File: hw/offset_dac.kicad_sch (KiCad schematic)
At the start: 23 parts, among them U11 TSV992A, U14 MCP47CVB02-E_UN

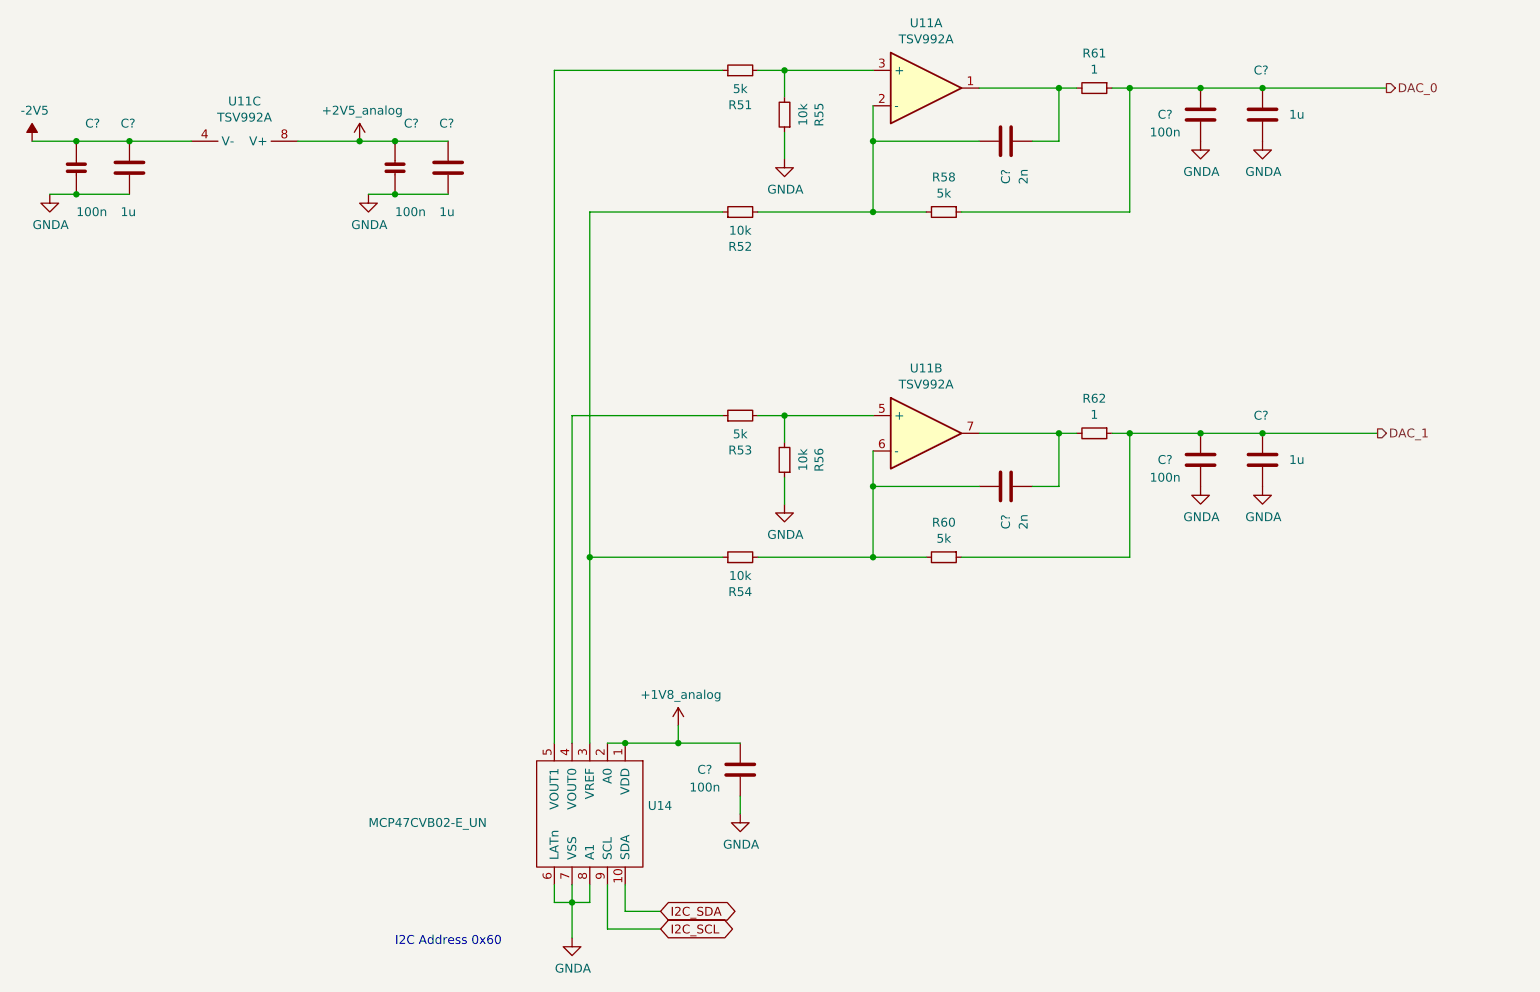
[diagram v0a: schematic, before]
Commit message: basic schematic, started layout (placing first components)
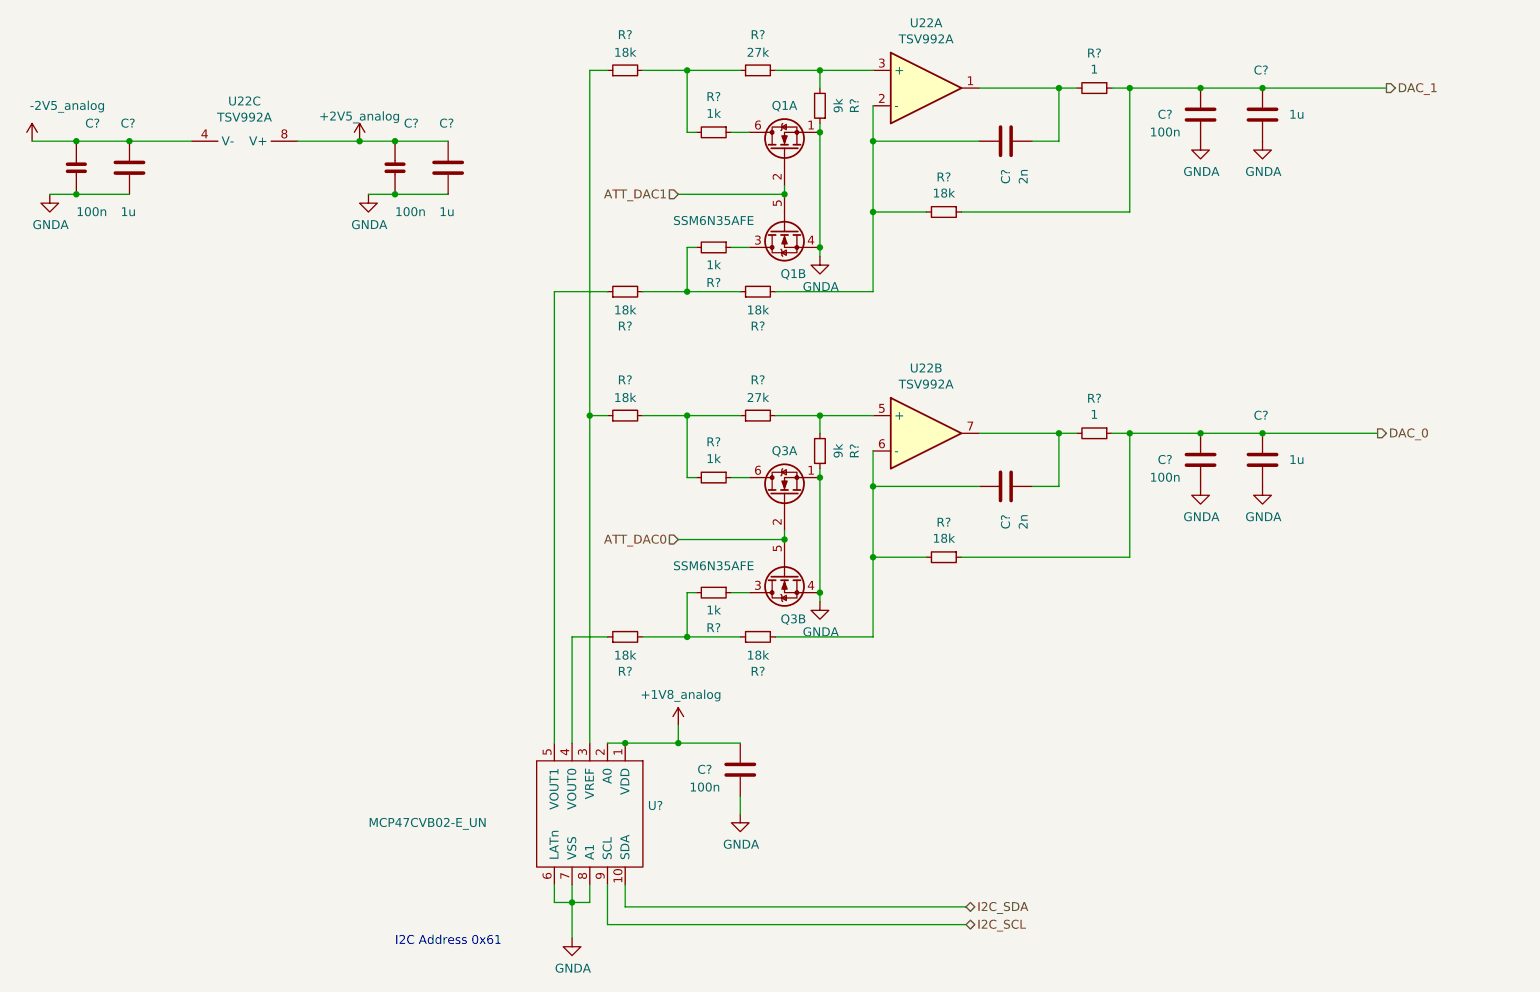
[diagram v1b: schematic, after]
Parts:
- removed R53: 5k, Resistor_SMD:R_0603_1608Metric, symbol Device:R_Small
- removed R54, R56: 10k, Resistor_SMD:R_0603_1608Metric, symbol Device:R_Small
- added Q1, Q3: SSM6N35AFE, proj_footprints:SOT-563-adjusted, symbol Device:Q_Dual_NMOS_S1G1D2S2G2D1
- added R? (x4): 1k, Resistor_SMD:R_0603_1608Metric, symbol Device:R_Small
- added R? (x4): 18k, Resistor_SMD:R_0603_1608Metric, symbol Device:R_Small
- added R? (x2): 27k, Resistor_SMD:R_0603_1608Metric, symbol Device:R_Small
- added R?: 9k, Resistor_SMD:R_0603_1608Metric, symbol Device:R_Small
- R?: renamed from R58; value 5k -> 18k
- R?: renamed from R55; value 10k -> 9k
- R?: renamed from R51; value 5k -> 18k
- R?: renamed from R52; value 10k -> 18k
- R?: renamed from R60; value 5k -> 18k
- U22: renamed from U11; symbol usbadc-rescue:Opamp_Dual_Generic-Device -> Device:Opamp_Dual
- renumbered R61 to R?, R62 to R?, U14 to U?
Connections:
- net DAC_0: now also C?.1, C?.2, R?.1, R?.1; no longer C?.1, C?.2, R?.1, R?.1
- net DAC_1: now also C?.1, C?.2, R?.1, R?.1; no longer C?.1, C?.2, R?.1, R?.1
- net GNDA: now also Q1.1 (S), Q1.4 (S), Q3.1 (S), Q3.4 (S), R?.1
- net at U?.3 (VREF): now also R?.1, R?.1; no longer R?.1
- net at U?.4 (VOUT0): now also R?.1
- net at U?.5 (VOUT1): now also R?.1; no longer R?.1
- net at C?.2, R?.2, U22.2 (-): now also R?.2; no longer R?.2
- net at R?.2, U22.3 (+): now also R?.2; no longer R?.2
- net at U22.5 (+): now also R?.2, R?.2
- net at C?.2, R?.2, U22.6 (-): now also R?.2
- net -2V5 renamed -2V5_analog
- new net: R?.1, R?.2, R?.2 (x4)
- new net: Q1.6 (D), R?.1
- new net: Q3.3 (D), R?.1
- new net: Q1.3 (D), R?.1
- new net: Q3.6 (D), R?.1
- new net ATT_DAC0: Q3.2 (G), Q3.5 (G)
- new net ATT_DAC1: Q1.2 (G), Q1.5 (G)
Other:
- note added: "I2C Address 0x61"
- note removed: "I2C Address 0x60"
- moved on the sheet: R?

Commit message: WIP - a lot already laid out.
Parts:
- C? (x2): footprint Capacitor_SMD:C_0402_1005Metric -> Capacitor_SMD:C_0603_1608Metric
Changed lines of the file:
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@@
       (effects (font (size 1.27 1.27)) (justify left))
     )
-    (property "Footprint" "Capacitor_SMD:C_0402_1005Metric" (at 78.4352 63.5 0)
+    (property "Footprint" "Capacitor_SMD:C_0603_1608Metric" (at 78.4352 63.5 0)
       (effects (font (size 1.27 1.27)) hide)
     )
@@
       (effects (font (size 1.27 1.27)) (justify left))
     )
-    (property "Footprint" "Capacitor_SMD:C_0402_1005Metric" (at 32.7152 63.5 0)
+    (property "Footprint" "Capacitor_SMD:C_0603_1608Metric" (at 32.7152 63.5 0)
       (effects (font (size 1.27 1.27)) hide)
     )

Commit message: finished routing; DRC passes (except for 1 hole violation at push-button)
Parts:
- C? (x2): Manufacturer Murata -> (none)
- C? (x3): Manufacturer Murata -> (none); Part GCJ188R71E104KA12D -> (none)
- C? (x4): Manufacturer Murata -> (none); Part GCJ219R71C105KA01 -> (none)
- C? (x2): Manufacturer Murata -> (none); Part GRM155R61C104KA88D -> (none)
- Q1, Q3: Manufacturer (none) -> Toshiba; Part (none) -> SSM6N35AFE
- Q1, Q3: Part (none) -> SSM6N35AFE
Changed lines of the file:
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@@
       (effects (font (size 1.27 1.27)) hide)
     )
-    (property "Manufacturer" "Murata" (at 172.72 61.595 0)
+    (property "Manufacturer" "" (at 172.72 61.595 0)
       (effects (font (size 1.27 1.27)) hide)
     )
@@
       (effects (font (size 1.27 1.27)) hide)
     )
-    (property "Part" "GCJ188R71E104KA12D" (at 189.865 57.15 0)
-      (effects (font (size 1.27 1.27)) hide)
-    )
-    (property "Manufacturer" "Murata" (at 187.325 59.69 0)
+    (property "Part" "" (at 189.865 57.15 0)
+      (effects (font (size 1.27 1.27)) hide)
+    )
+    (property "Manufacturer" "" (at 187.325 59.69 0)
       (effects (font (size 1.27 1.27)) hide)
     )
@@
       (effects (font (size 1.27 1.27)) hide)
     )
-    (property "Part" "GCJ219R71C105KA01" (at 205.105 46.99 0)
-      (effects (font (size 1.27 1.27)) hide)
-    )
-    (property "Manufacturer" "Murata" (at 207.645 44.45 0)
+    (property "Part" "" (at 205.105 46.99 0)
+      (effects (font (size 1.27 1.27)) hide)
+    )
+    (property "Manufacturer" "" (at 207.645 44.45 0)
       (effects (font (size 1.27 1.27)) hide)
     )
@@
       (effects (font (size 1.27 1.27)) hide)
     )
-    (property "Manufacturer" "Murata" (at 172.72 111.125 0)
+    (property "Manufacturer" "" (at 172.72 111.125 0)
       (effects (font (size 1.27 1.27)) hide)
     )
@@
       (effects (font (size 1.27 1.27)) hide)
     )
-    (property "Part" "GCJ188R71E104KA12D" (at 189.865 106.68 0)
-      (effects (font (size 1.27 1.27)) hide)
-    )
-    (property "Manufacturer" "Murata" (at 187.325 109.22 0)
+    (property "Part" "" (at 189.865 106.68 0)
+      (effects (font (size 1.27 1.27)) hide)
+    )
+    (property "Manufacturer" "" (at 187.325 109.22 0)
       (effects (font (size 1.27 1.27)) hide)
     )
@@
       (effects (font (size 1.27 1.27)) hide)
     )
-    (property "Part" "GCJ219R71C105KA01" (at 205.105 96.52 0)
-      (effects (font (size 1.27 1.27)) hide)
-    )
-    (property "Manufacturer" "Murata" (at 207.645 93.98 0)
+    (property "Part" "" (at 205.105 96.52 0)
+      (effects (font (size 1.27 1.27)) hide)
+    )
+    (property "Manufacturer" "" (at 207.645 93.98 0)
       (effects (font (size 1.27 1.27)) hide)
     )
@@
       (effects (font (size 1.27 1.27)) hide)
     )
-    (property "Part" "GCJ188R71E104KA12D" (at 123.825 151.13 0)
-      (effects (font (size 1.27 1.27)) hide)
-    )
-    (property "Manufacturer" "Murata" (at 121.285 153.67 0)
+    (property "Part" "" (at 123.825 151.13 0)
+      (effects (font (size 1.27 1.27)) hide)
+    )
+    (property "Manufacturer" "" (at 121.285 153.67 0)
       (effects (font (size 1.27 1.27)) hide)
     )
@@
       (effects (font (size 1.27 1.27)) hide)
     )
-    (property "Part" "GRM155R61C104KA88D" (at 80.645 54.61 0)
-      (effects (font (size 1.27 1.27)) hide)
-    )
-    (property "Manufacturer" "Murata" (at 83.185 52.07 0)
+    (property "Part" "" (at 80.645 54.61 0)
+      (effects (font (size 1.27 1.27)) hide)
+    )
+    (property "Manufacturer" "" (at 83.185 52.07 0)
       (effects (font (size 1.27 1.27)) hide)
     )
@@
       (effects (font (size 1.27 1.27)) hide)
     )
-    (property "Part" "GCJ219R71C105KA01" (at 88.265 54.61 0)
-      (effects (font (size 1.27 1.27)) hide)
-    )
-    (property "Manufacturer" "Murata" (at 90.805 52.07 0)
+    (property "Part" "" (at 88.265 54.61 0)
+      (effects (font (size 1.27 1.27)) hide)
+    )
+    (property "Manufacturer" "" (at 90.805 52.07 0)
       (effects (font (size 1.27 1.27)) hide)
     )
@@
       (effects (font (size 1.27 1.27)) hide)
     )
-    (property "Part" "GRM155R61C104KA88D" (at 34.925 54.61 0)
-      (effects (font (size 1.27 1.27)) hide)
-    )
-    (property "Manufacturer" "Murata" (at 37.465 52.07 0)
+    (property "Part" "" (at 34.925 54.61 0)
+      (effects (font (size 1.27 1.27)) hide)
+    )
+    (property "Manufacturer" "" (at 37.465 52.07 0)
       (effects (font (size 1.27 1.27)) hide)
     )
@@
       (effects (font (size 1.27 1.27)) hide)
     )
-    (property "Part" "GCJ219R71C105KA01" (at 42.545 54.61 0)
-      (effects (font (size 1.27 1.27)) hide)
-    )
-    (property "Manufacturer" "Murata" (at 45.085 52.07 0)
+    (property "Part" "" (at 42.545 54.61 0)
+      (effects (font (size 1.27 1.27)) hide)
+    )
+    (property "Manufacturer" "" (at 45.085 52.07 0)
       (effects (font (size 1.27 1.27)) hide)
     )
@@
     )
     (property "Datasheet" "~" (at 133.35 52.07 0)
+      (effects (font (size 1.27 1.27)) hide)
+    )
+    (property "Manufacturer" "Toshiba" (at 133.35 57.15 0)
+      (effects (font (size 1.27 1.27)) hide)
+    )
+    (property "Part" "SSM6N35AFE" (at 133.35 57.15 0)
       (effects (font (size 1.27 1.27)) hide)
     )
@@
       (effects (font (size 1.27 1.27)) hide)
     )
+    (property "Manufacturer" "Toshiba" (at 133.35 106.68 0)
+      (effects (font (size 1.27 1.27)) hide)
+    )
+    (property "Part" "SSM6N35AFE" (at 133.35 106.68 0)
+      (effects (font (size 1.27 1.27)) hide)
+    )
     (pin "1")
     (pin "2")
@@
       (effects (font (size 1.27 1.27)) hide)
     )
+    (property "Part" "SSM6N35AFE" (at 133.35 68.58 0)
+      (effects (font (size 1.27 1.27)) hide)
+    )
     (pin "1")
     (pin "2")
@@
       (effects (font (size 1.27 1.27)) hide)
     )
+    (property "Part" "SSM6N35AFE" (at 133.35 118.11 0)
+      (effects (font (size 1.27 1.27)) hide)
+    )

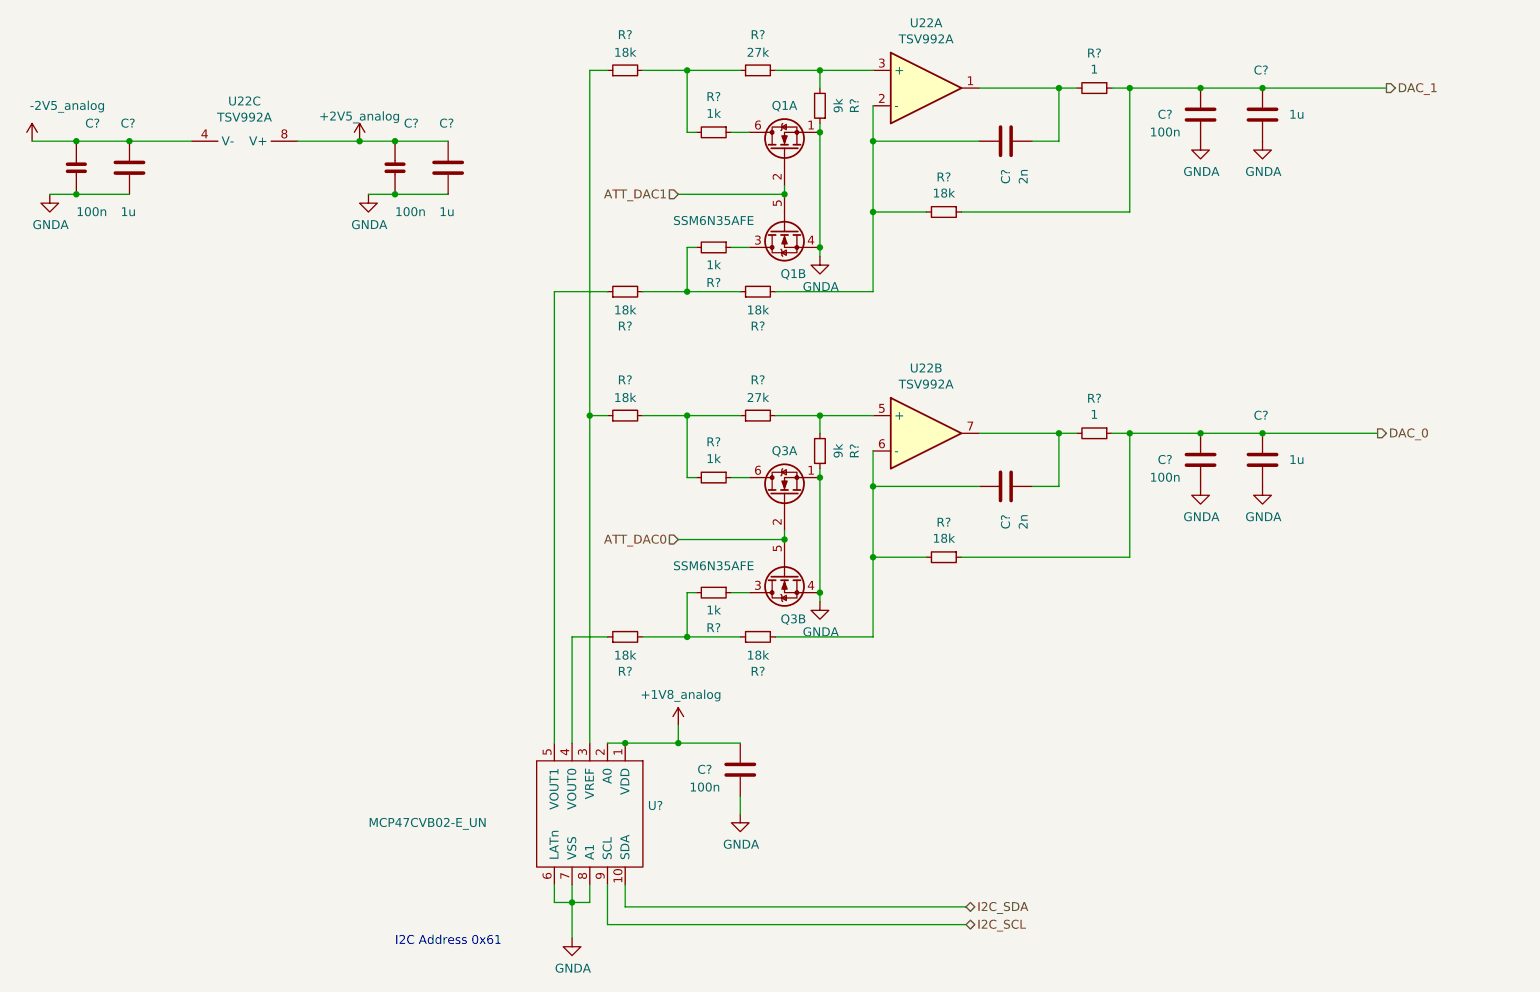
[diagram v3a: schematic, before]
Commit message: Added trion top-sheet as sub-sheet to usbadc project
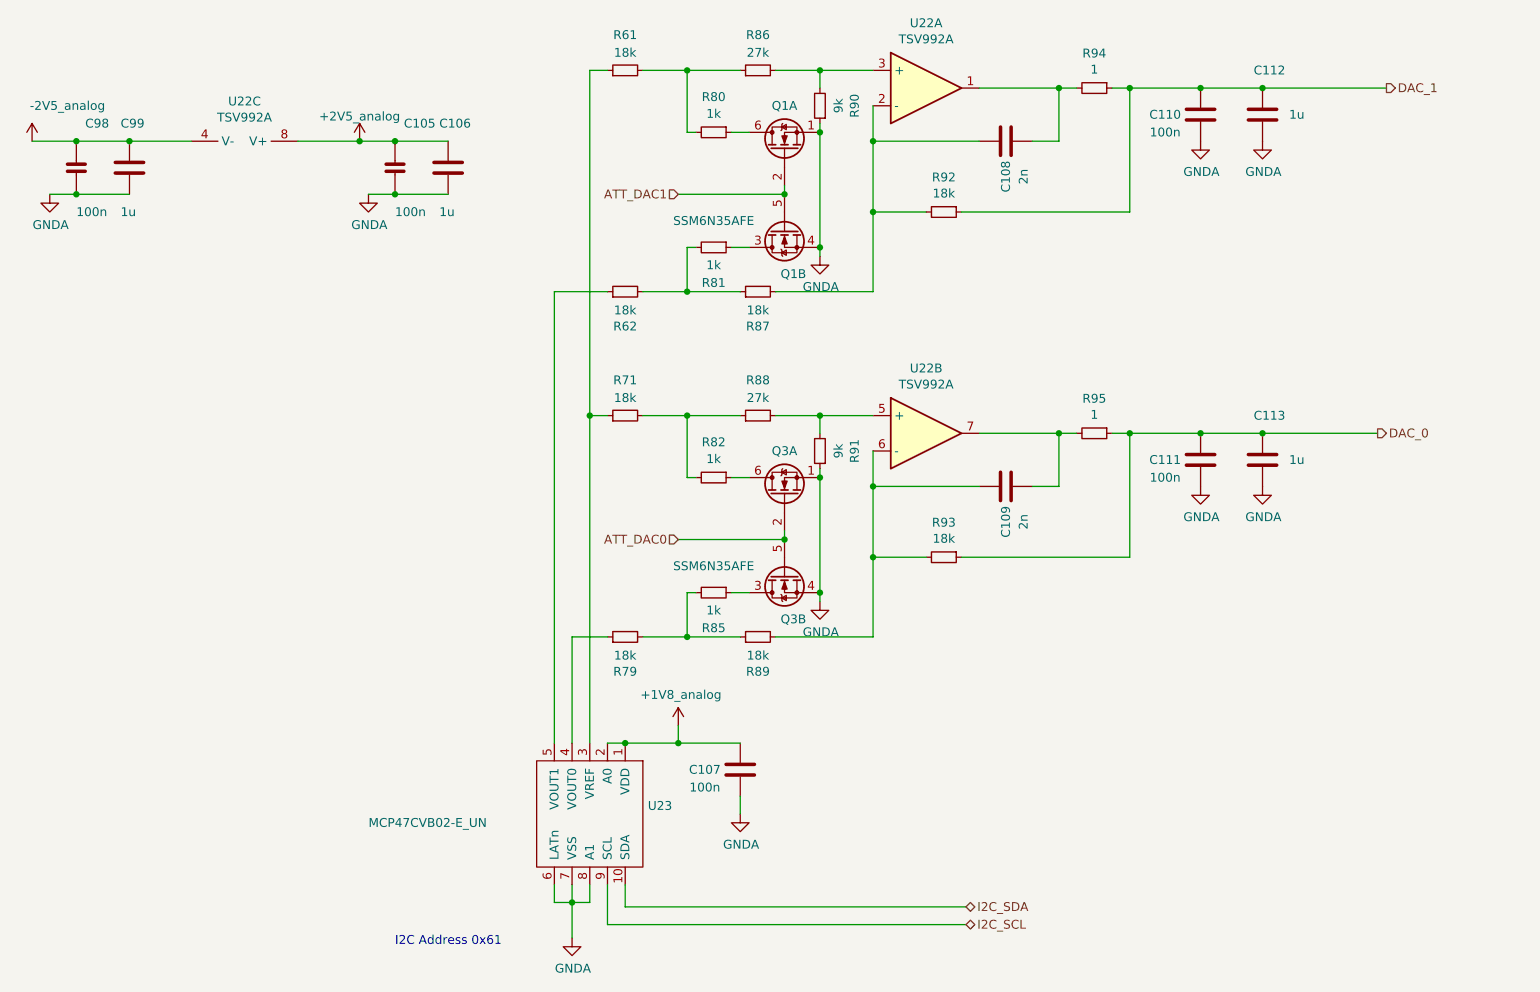
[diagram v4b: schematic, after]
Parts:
- gave numbers to parts that had none: 30
